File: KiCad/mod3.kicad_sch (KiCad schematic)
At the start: 49 parts, among them M5 Fan_4pin, M6 Fan_4pin, U3 ZD25Q64BSIGT

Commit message: Finish connecting x1 slot. Add pcie clkreq lines
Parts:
- removed R54, R55: 10k, Resistor_SMD:R_0402_1005Metric, symbol Device:R_Small
- added R12: 10k, Resistor_SMD:R_0402_1005Metric, symbol Device:R_Small
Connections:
- net M2_EKEY.REFCLK+ is gone; now on net NVME.REFCLK+: A3.97 (REFCLK2+)
- net M2_EKEY.REFCLK- is gone; now on net NVME.REFCLK-: A3.99 (REFCLK2-)
- net ETH.REFCLK+: now also A3.88 (REFCLK3+); no longer A3.85 (REFCLK0+)
- net ETH.REFCLK-: now also A3.90 (REFCLK3-); no longer A3.87 (REFCLK0-)
- net GND: now also R12.2
- net NVME.REFCLK+: no longer A3.91 (REFCLK1+)
- net NVME.REFCLK-: no longer A3.93 (REFCLK1-)
- net at A3.102 (~{CLKREQ4}): now also R12.1
- net ETH.~{CLKREQ}: now reaches A3.100 (~{CLKREQ3})
- net PCIE_X1.REFCLK+: now reaches A3.94 (REFCLK4+)
- net PCIE_X1.REFCLK-: now reaches A3.96 (REFCLK4-)
- net M2_EKEY.Rx0+ renamed PCIE_X1.Rx0+
- net M2_EKEY.Rx0- renamed PCIE_X1.Rx0-
- net M2_EKEY.SUSCLK renamed NVME.SUSCLK
- net M2_EKEY.Tx0+ renamed PCIE_X1.Tx0+
- net M2_EKEY.Tx0- renamed PCIE_X1.Tx0-
- net M2_EKEY.USB-D+ renamed PCIE_X1.USB-D+
- net M2_EKEY.USB-D- renamed PCIE_X1.USB-D-

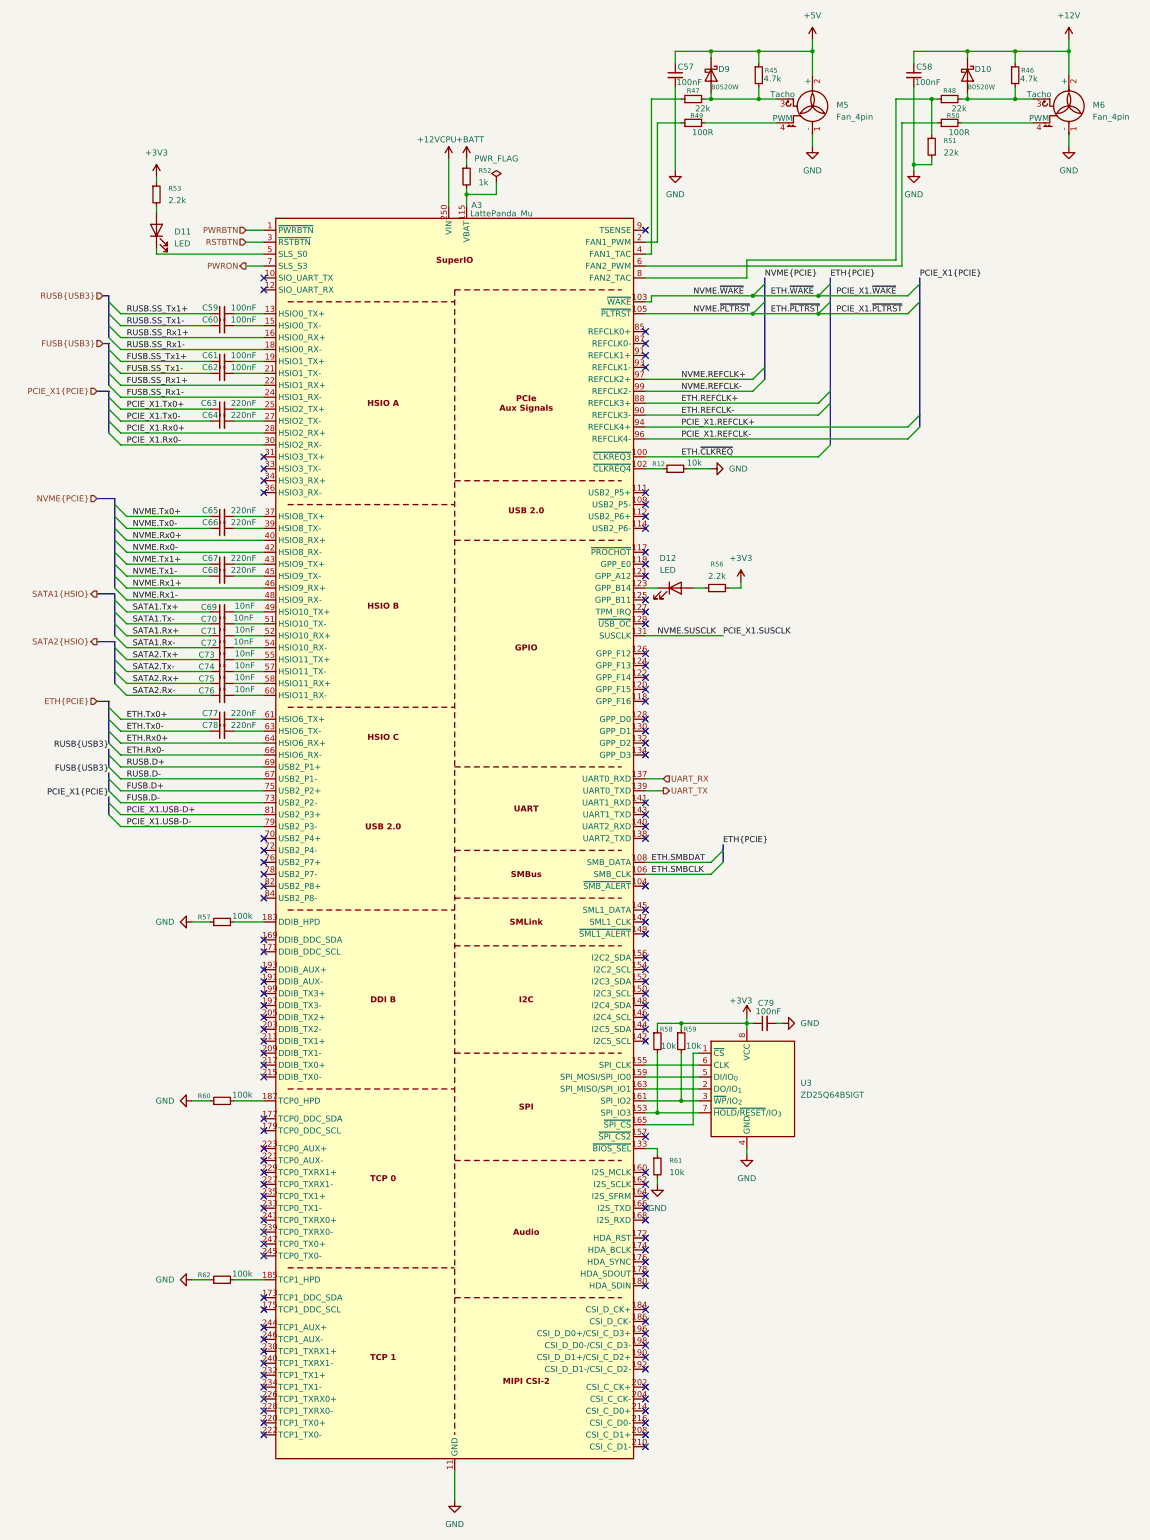
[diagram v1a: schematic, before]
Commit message: Re-annotate schematic
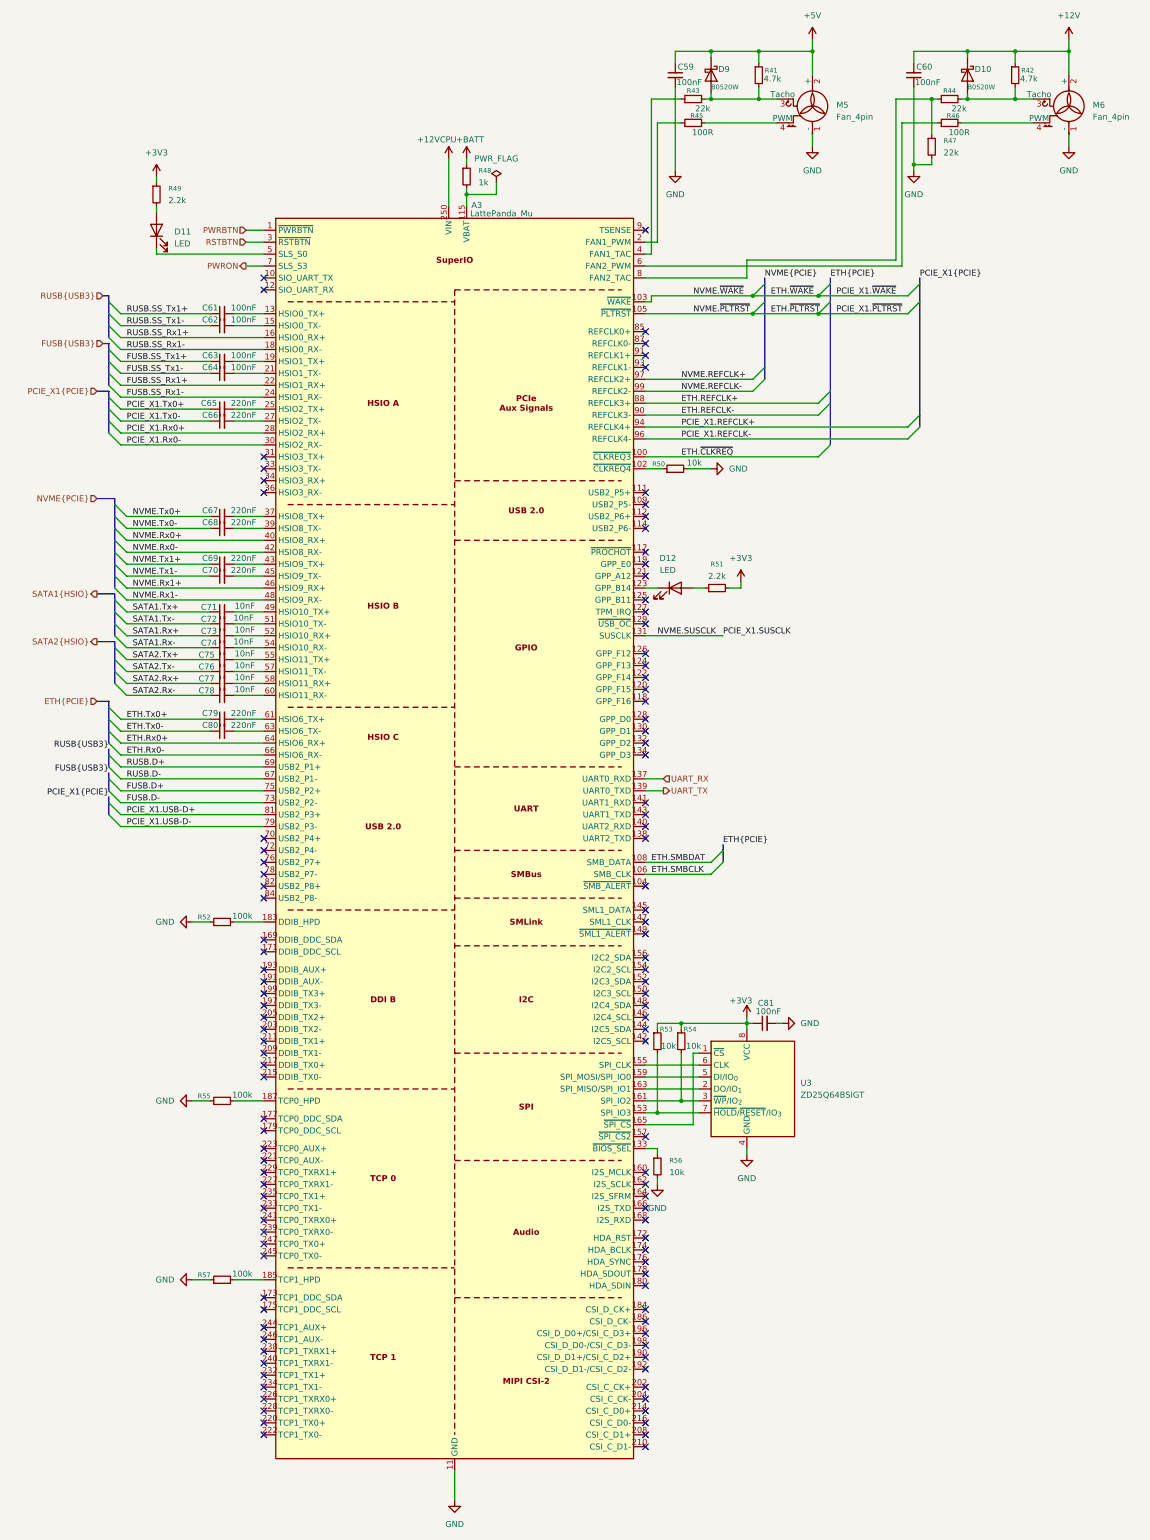
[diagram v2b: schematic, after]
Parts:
- renumbered C57 to C59, C58 to C60, C59 to C61, C60 to C62, C61 to C63, C62 to C64, C63 to C65, C64 to C66, C65 to C67, C66 to C68, C67 to C69, C68 to C70, C69 to C71, C70 to C72, C71 to C73, C72 to C74, C73 to C75, C74 to C76, C75 to C77, C76 to C78, C77 to C79, C78 to C80, C79 to C81, R45 to R41, R46 to R42, R47 to R43, R48 to R44, R49 to R45, R50 to R46, R51 to R47, R52 to R48, R53 to R49, R12 to R50, R56 to R51, R57 to R52, R58 to R53, R59 to R54, R60 to R55, R61 to R56, R62 to R57

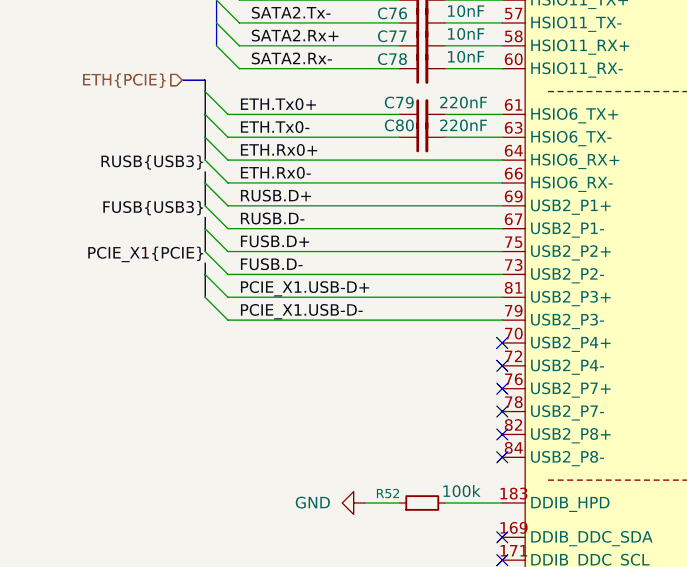
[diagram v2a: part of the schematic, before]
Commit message: change sata symbols
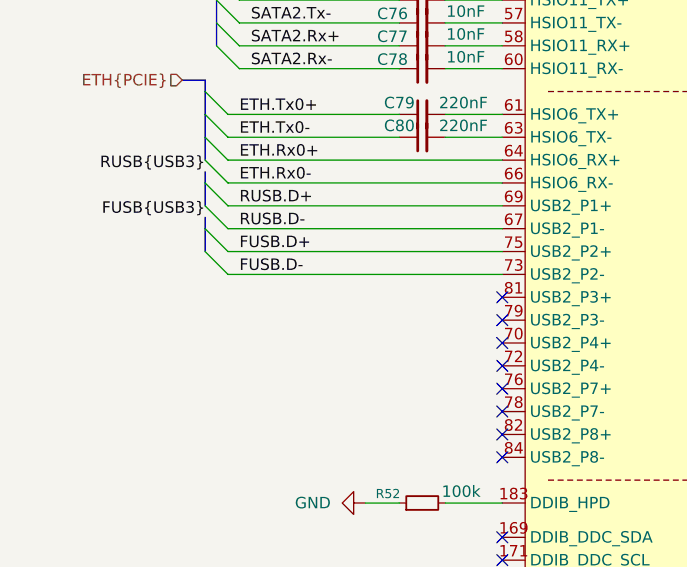
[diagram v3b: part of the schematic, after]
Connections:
- net PCIE_X1.USB-D+: no longer names the net of A3.81 (USB2_P3+)
- net PCIE_X1.USB-D-: no longer names the net of A3.79 (USB2_P3-)
- no-connect marks 111 -> 113
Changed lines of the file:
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@@
 	)
 	(no_connect
+		(at 232.41 204.47)
+	)
+	(no_connect
 		(at 232.41 285.75)
 	)
@@
 	)
 	(no_connect
+		(at 232.41 201.93)
+	)
+	(no_connect
 		(at 313.69 101.6)
 	)
@@
 	)
 	(bus_entry
-		(at 199.39 199.39)
-		(size 2.54 2.54)
-		(stroke
-			(width 0)
-			(type default)
-		)
-	)
-	(bus_entry
 		(at 199.39 184.15)
 		(size 2.54 2.54)
@@
 		)
 	)
-	(bus_entry
-		(at 199.39 201.93)
-		(size 2.54 2.54)
-		(stroke
-			(width 0)
-			(type default)
-		)
-	)
 	(wire
 		(pts
@@
 	(bus
 		(pts
-			(xy 199.39 198.12) (xy 199.39 199.39)
-		)
-		(stroke
-			(width 0)
-			(type default)
-		)
-	)
-	(bus
-		(pts
 			(xy 196.85 134.62) (xy 200.66 134.62)
 		)
@@
 	(wire
 		(pts
-			(xy 201.93 204.47) (xy 232.41 204.47)
-		)
-		(stroke
-			(width 0)
-			(type default)
-		)
-	)
-	(wire
-		(pts
 			(xy 281.94 69.85) (xy 275.59 69.85)
 		)
@@
 		)
 	)
-	(bus
-		(pts
-			(xy 199.39 199.39) (xy 199.39 201.93)
-		)
-		(stroke
-			(width 0)
-			(type default)
-		)
-	)
 	(wire
 		(pts
@@
 	(wire
 		(pts
-			(xy 201.93 201.93) (xy 232.41 201.93)
-		)
-		(stroke
-			(width 0)
-			(type default)
-		)
-	)
-	(wire
-		(pts
 			(xy 275.59 68.58) (xy 275.59 69.85)
 		)
@@
 		)
 	)
-	(label "PCIE_X1.USB-D-"
-		(at 203.2 204.47 0)
-		(effects
-			(font
-				(size 1.27 1.27)
-			)
-			(justify left bottom)
-		)
-	)
 	(label "SATA2.Rx-"
 		(at 204.47 176.53 0)
@@
 		)
 	)
-	(label "PCIE_X1{PCIE}"
-		(at 199.39 198.12 180)
-		(effects
-			(font
-				(size 1.27 1.27)
-			)
-			(justify right bottom)
-		)
-	)
 	(label "NVME.SUSCLK"
 		(at 316.23 163.83 0)
@@
 		(effects
 			(font
-				(size 1.27 1.27)
-			)
-			(justify left bottom)
-		)
-	)
-	(label "PCIE_X1.USB-D+"
-		(at 203.2 201.93 0)
-		(effects
-			(font
